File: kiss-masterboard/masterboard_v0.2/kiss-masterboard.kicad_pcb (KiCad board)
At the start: 2 copper layers, 187 x 152 mm, 185 parts, among them J1 Cubebatt_host, J10 CRESET, J11 Jumper, J12 Jumper, J13 Conn_02x08_Odd_Even, J14 Conn_02x08_Odd_Even, J15 jmp, J16 jmp, J17 gain_jumper, J18 Speaker, J2 Conn_01x02, J3 Conn_01x02, J4 Conn_01x02, J5 Conn_01x02, J6 Conn_01x02, J7 Conn_01x02, J8 Jumper, J9 jmp, P2 CONN_02X20, U1 TPS54327, U10 CSD86360Q5D, U12 1V2, U13 SN74LVC8T245, U14 W25Q, U15 MPU-9250, U16 ADS1000, U17 12MHz, U2 SN74LVC8T245, U3 3.3V, U4 ICE40UP5k-SG48, U5 SN74LVC8T245, U6 MAX98357, U7 SPH0645LM4H, U9 TPS53819A

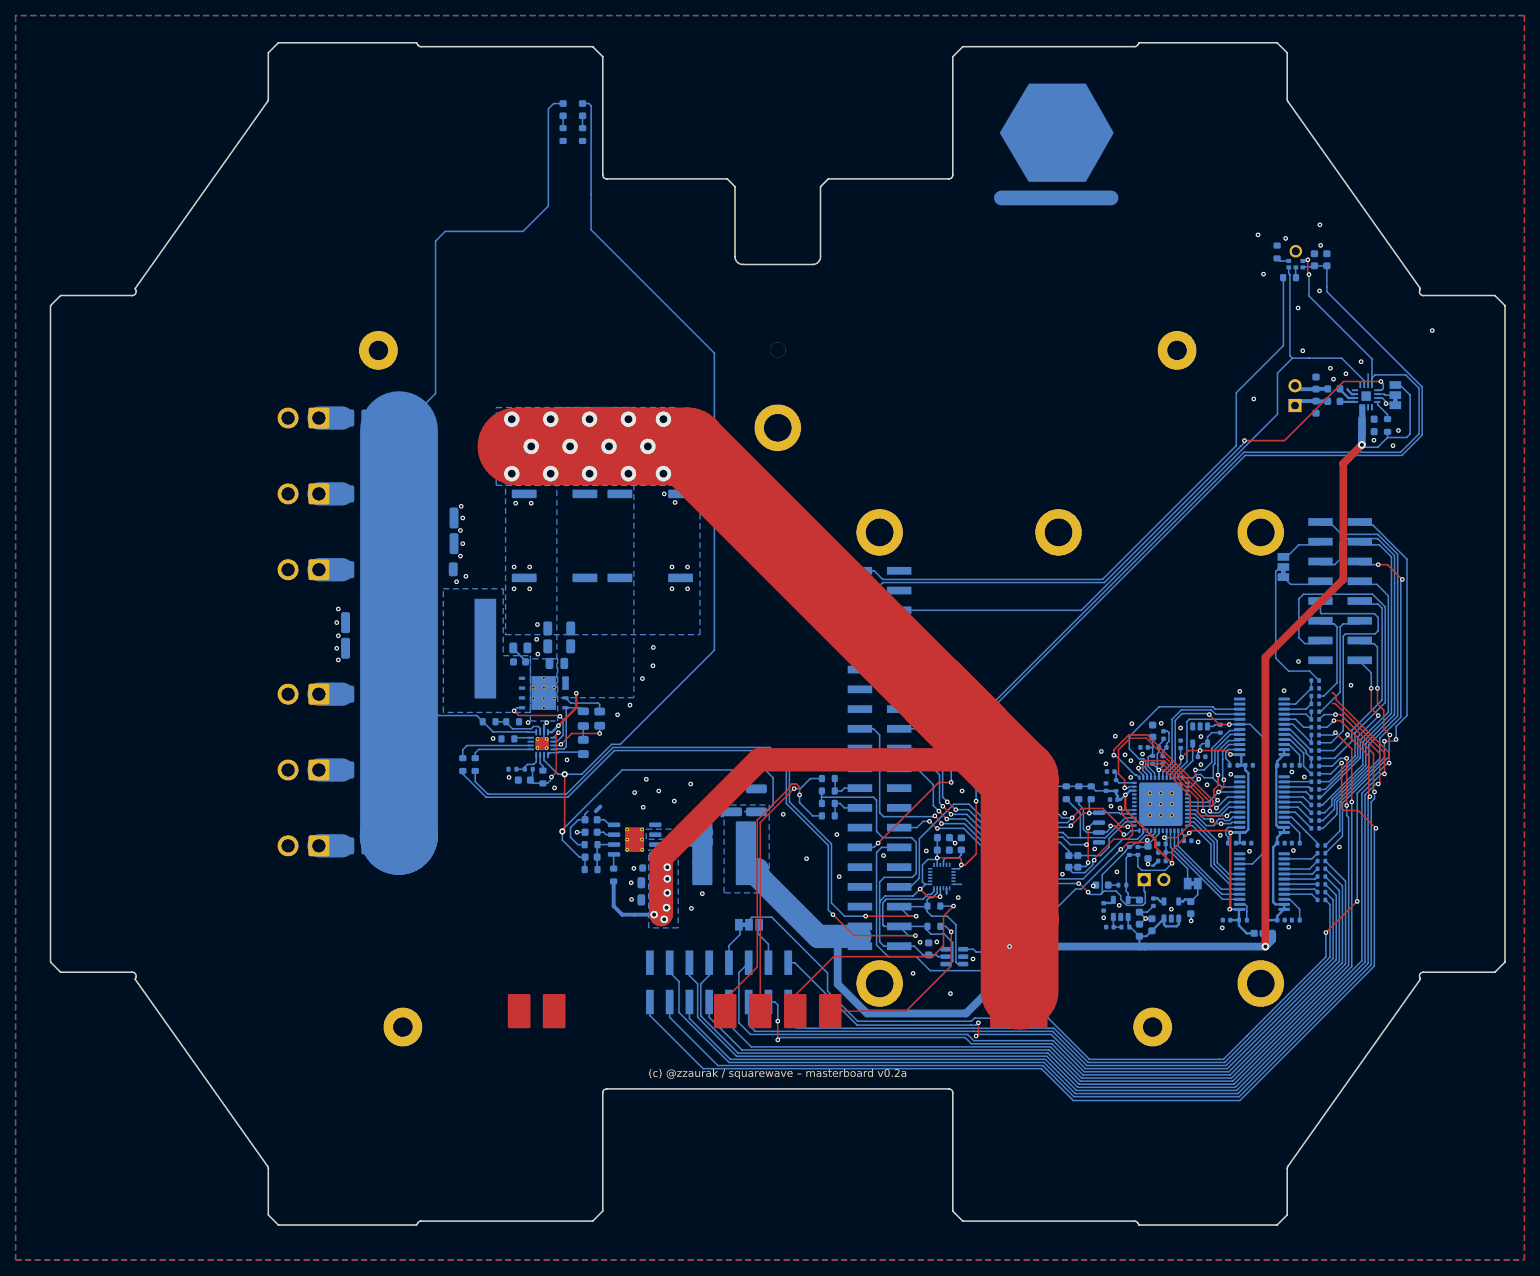
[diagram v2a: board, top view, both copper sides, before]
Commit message: replaced symbosl with standart symbols and reduced DRC errorsMAX98357A and TLV75709PDBV symbols
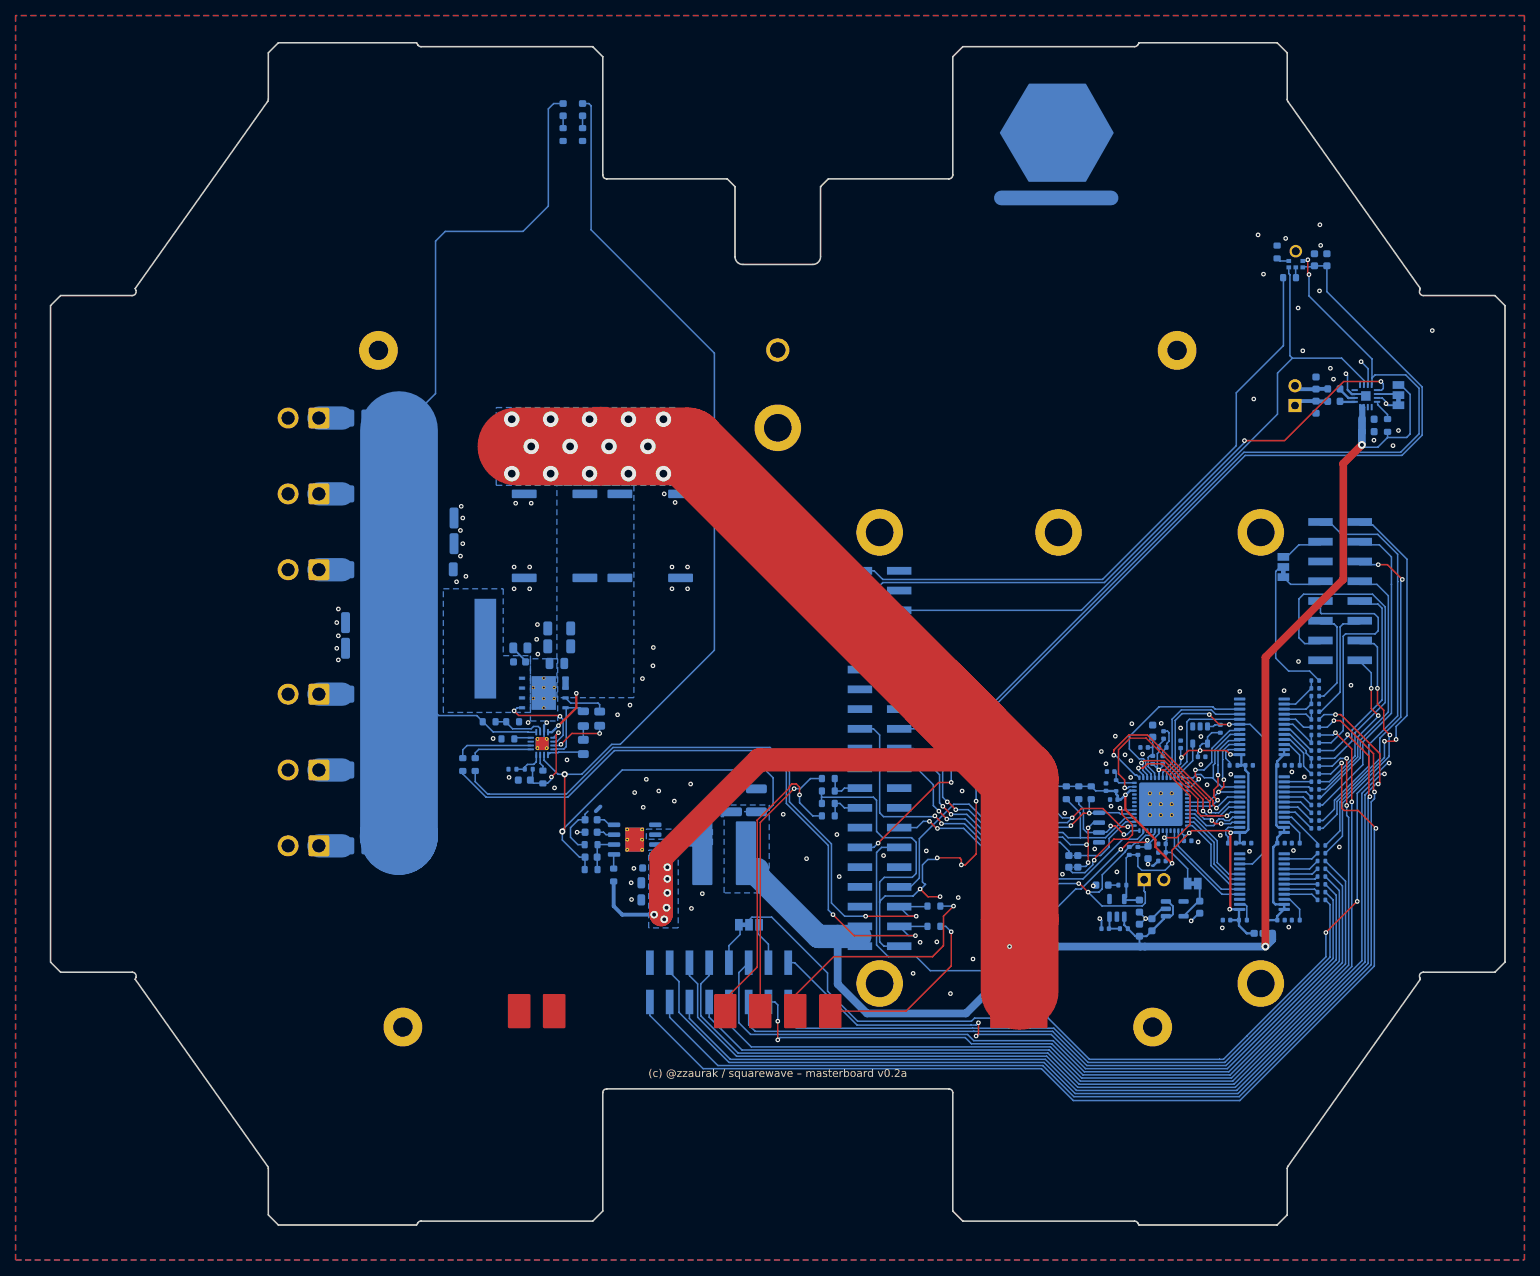
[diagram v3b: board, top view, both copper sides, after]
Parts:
- removed C20, C27: 10n, Capacitor_SMD:C_0402_1005Metric
- removed C66: 10nF, Capacitor_SMD:C_0603_1608Metric
- removed C67, C68, C69: 100nF, Capacitor_SMD:C_0603_1608Metric
- removed J17: gain_jumper, Jumper:SolderJumper-3_P1.3mm_Bridged12_Pad1.0x1.5mm_NumberLabels
- removed R49: 10K 1%, Resistor_SMD:R_0603_1608Metric
- removed R50: 1.78K 1%, Resistor_SMD:R_0603_1608Metric
- removed U12: 1V2, pkl_housings_sot:SOT-23-5
- removed U15: MPU-9250, Sensor_Motion:InvenSense_QFN-24_3x3mm_P0.4mm
- removed U16: ADS1000, Package_TO_SOT_SMD:SOT-23-6
- removed U6: MAX98357, Package_DFN_QFN:TQFN-16-1EP_3x3mm_P0.5mm_EP1.23x1.23mm
- added J19: gain_jumper, Jumper:SolderJumper-3_P1.3mm_Bridged12_Pad1.0x1.5mm_NumberLabels, B.Cu at (187.8, 58.8)
- added U11: TLV75733PDBV, Package_TO_SOT_SMD:SOT-23-5, B.Cu at (151.6, 124.7)
- added U8: TLV75709PDBV, Package_TO_SOT_SMD:SOT-23-5, B.Cu at (159.0, 124.8)
- U3: value 3.3V -> MAX98357A; footprint pkl_housings_sot:SOT-23-5 -> Package_DFN_QFN:TQFN-16-1EP_3x3mm_P0.5mm_EP1.23x1.23mm
- moved U3 73.0 mm to (183.6, 58.9), turned to 180 degrees
- moved C54 1.15 mm to (162.3, 124.6)
- moved C14 0.63 mm to (150.1, 127.4)
- moved R16 0.28 mm to (152.5, 127.4)
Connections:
- C14 pad 1: Net-(U3-EN) -> Net-(U11-EN)
- FB1 pad 2: Net-(U6-OUTP) -> Net-(U3-OUTP)
- FB2 pad 2: Net-(U6-OUTN) -> Net-(U3-OUTN)
- R16 pad 2: Net-(U3-EN) -> Net-(U11-EN)
- R33 pad 1: Net-(U6-~{SD_MODE}) -> Net-(U3-~{SD_MODE})
- U3 pad 1: /5V_switched -> /Digital Audio/DIN
- U3 pad 2: GND -> Net-(J19-C)
- U3 pad 3: Net-(U3-EN) -> GND
- U3 pad 4: Net-(U3-BYP) -> Net-(U3-~{SD_MODE})
- U3 pad 5: +3V3 -> unconnected-(U3-NC-Pad5)
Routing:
- net /FPGA Panel Driver/P2_G1x: track 50.5 -> 0.00 mm
- net /SDA: track 106.8 -> 85.7 mm
- net /SCL: track 97.6 -> 83.6 mm
- net /FPGA Panel Driver/P1_A4x: track 131.4 -> 117.5 mm
- net /FPGA Panel Driver/P1_iR0: track 13.8 -> 0.00 mm
- net /Raspberry Pi/3v3: track 192.3 -> 178.7 mm
- net /FPGA Panel Driver/P1_A3x: track 140.8 -> 128.8 mm
- net Net-(U16-VIN+): track 4.63 -> 0.00 mm
- net /Power_switched: track 197.1 -> 192.9 mm
- net Net-(U15-REGOUT): track 3.80 -> 0.00 mm
- net Net-(U1-SW): track 6.47 -> 2.87 mm
- net GND: track 31.6 -> 34.9 mm, vias 121 -> 118
- net Net-(U11-EN): track 0.00 -> 2.88 mm
- net Net-(U6-~{SD_MODE}): track 2.77 -> 0.00 mm
- net Net-(U3-~{SD_MODE}): track 0.00 -> 2.77 mm
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
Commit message: Fix DRC issues
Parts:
- removed LG1: Logo_DOT1, logos:Logo_Dot_15mm_Text_Mask
- removed LG2: Logo_Squarewave, logos:Logo_Squarewave_Text_15mm_Silks
- J11, J12: footprint pkl_jumpers:J_NC_0603_15 -> Jumper:SolderJumper-2_P1.3mm_Bridged2Bar_Pad1.0x1.5mm
- J9: footprint pkl_jumpers:J_NCNO_0903_30 -> Jumper:SolderJumper-3_P1.3mm_Bridged12_Pad1.0x1.5mm
- moved J12 1.50 mm to (146.0, 121.0)
- moved J11 0.40 mm to (146.0, 118.4)
- moved J9 0.20 mm to (170.4, 128.2)
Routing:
- net /FPGA Panel Driver/P2_G1x: track 0.00 -> 44.0 mm, vias 0 -> 2
- net /FPGA Panel Driver/P1_A4x: track 117.5 -> 131.2 mm, vias 3 -> 4
- net /FPGA Panel Driver/P1_iR0: track 0.00 -> 13.7 mm
- net /FPGA Panel Driver/P1_A3x: track 128.8 -> 142.4 mm, vias 1 -> 2
- net /Raspberry Pi/3v3: track 178.7 -> 171.1 mm, vias 5 -> 2
- net GND: track 34.9 -> 38.8 mm, vias 118 -> 117
- net /FPGA Panel Driver/FPGA_SS_PANEL: track 53.2 -> 55.0 mm
- net /FPGA Panel Driver/FLASH_MISO|IO1: track 39.3 -> 40.3 mm
- net /FPGA Panel Driver/P2_B0x: track 40.7 -> 40.0 mm
- net /FPGA Panel Driver/P2_A2x: track 14.8 -> 15.5 mm
- net /Power_switched: track 192.9 -> 192.7 mm, vias 23 -> 22

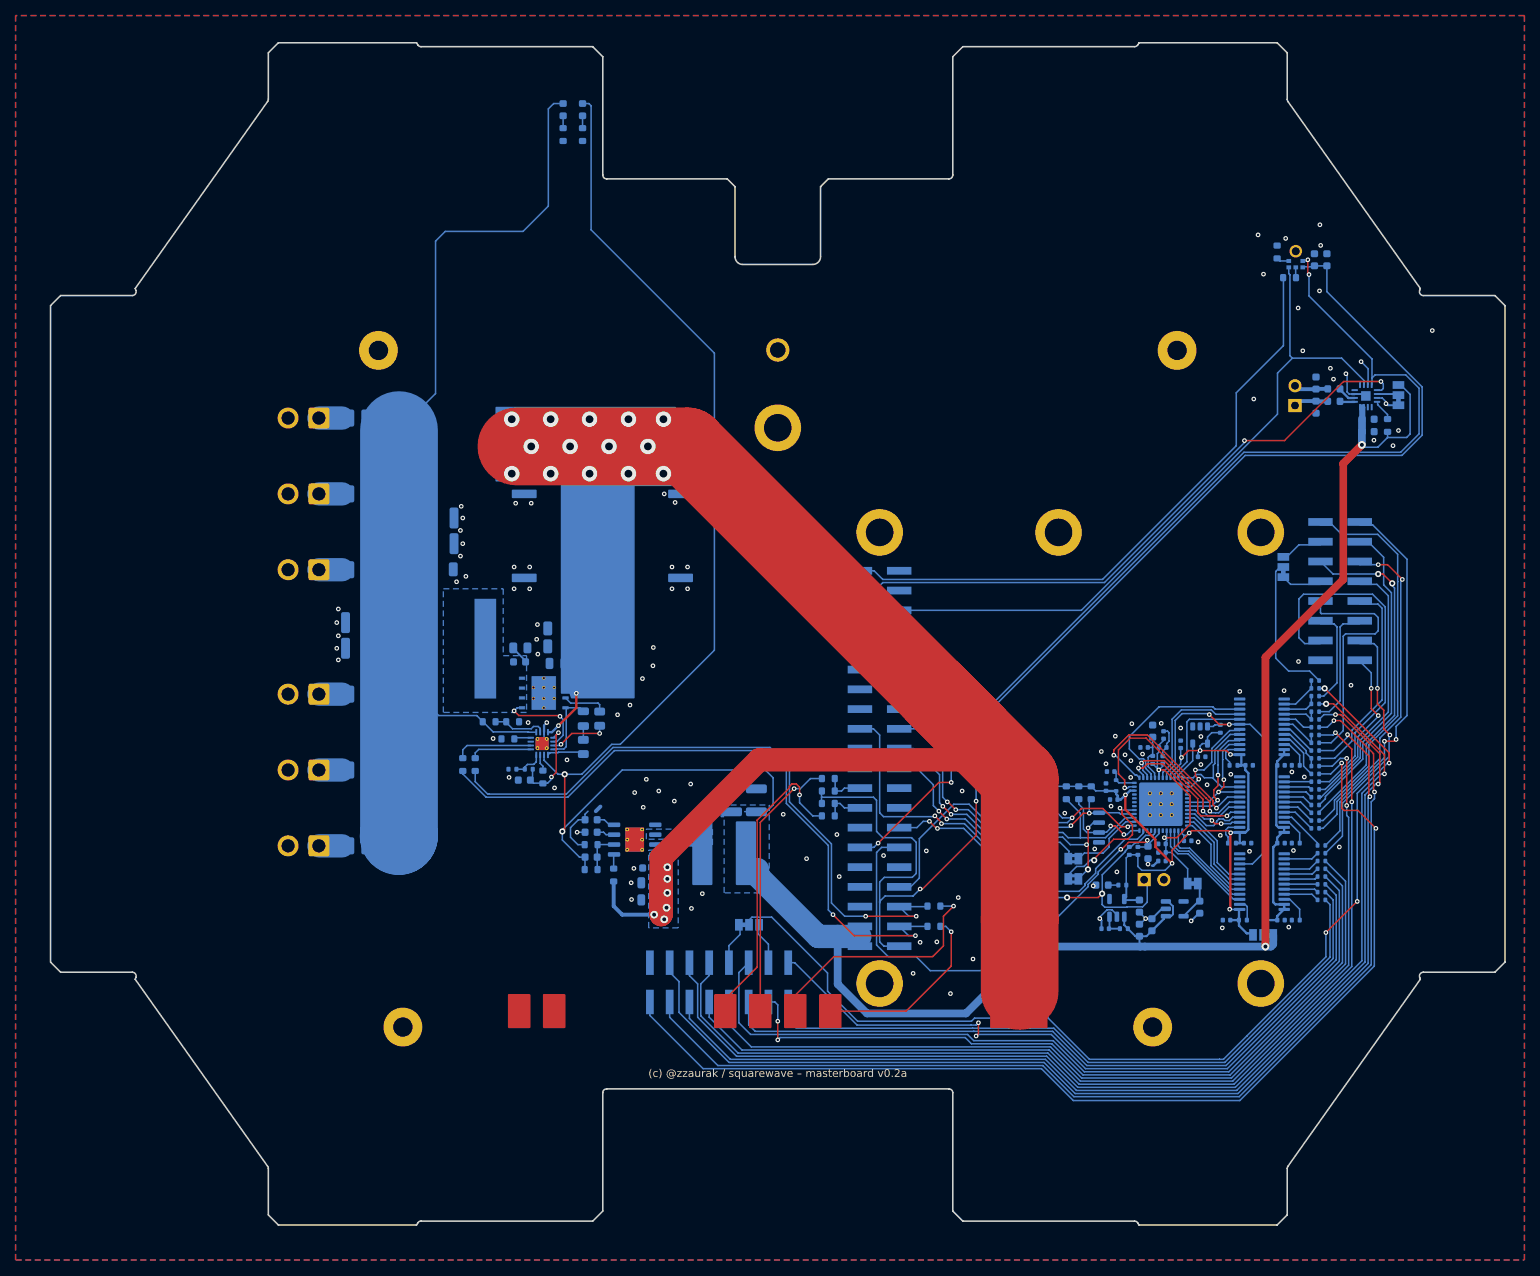
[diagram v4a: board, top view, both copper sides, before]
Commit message: Adjust to new batterypack,
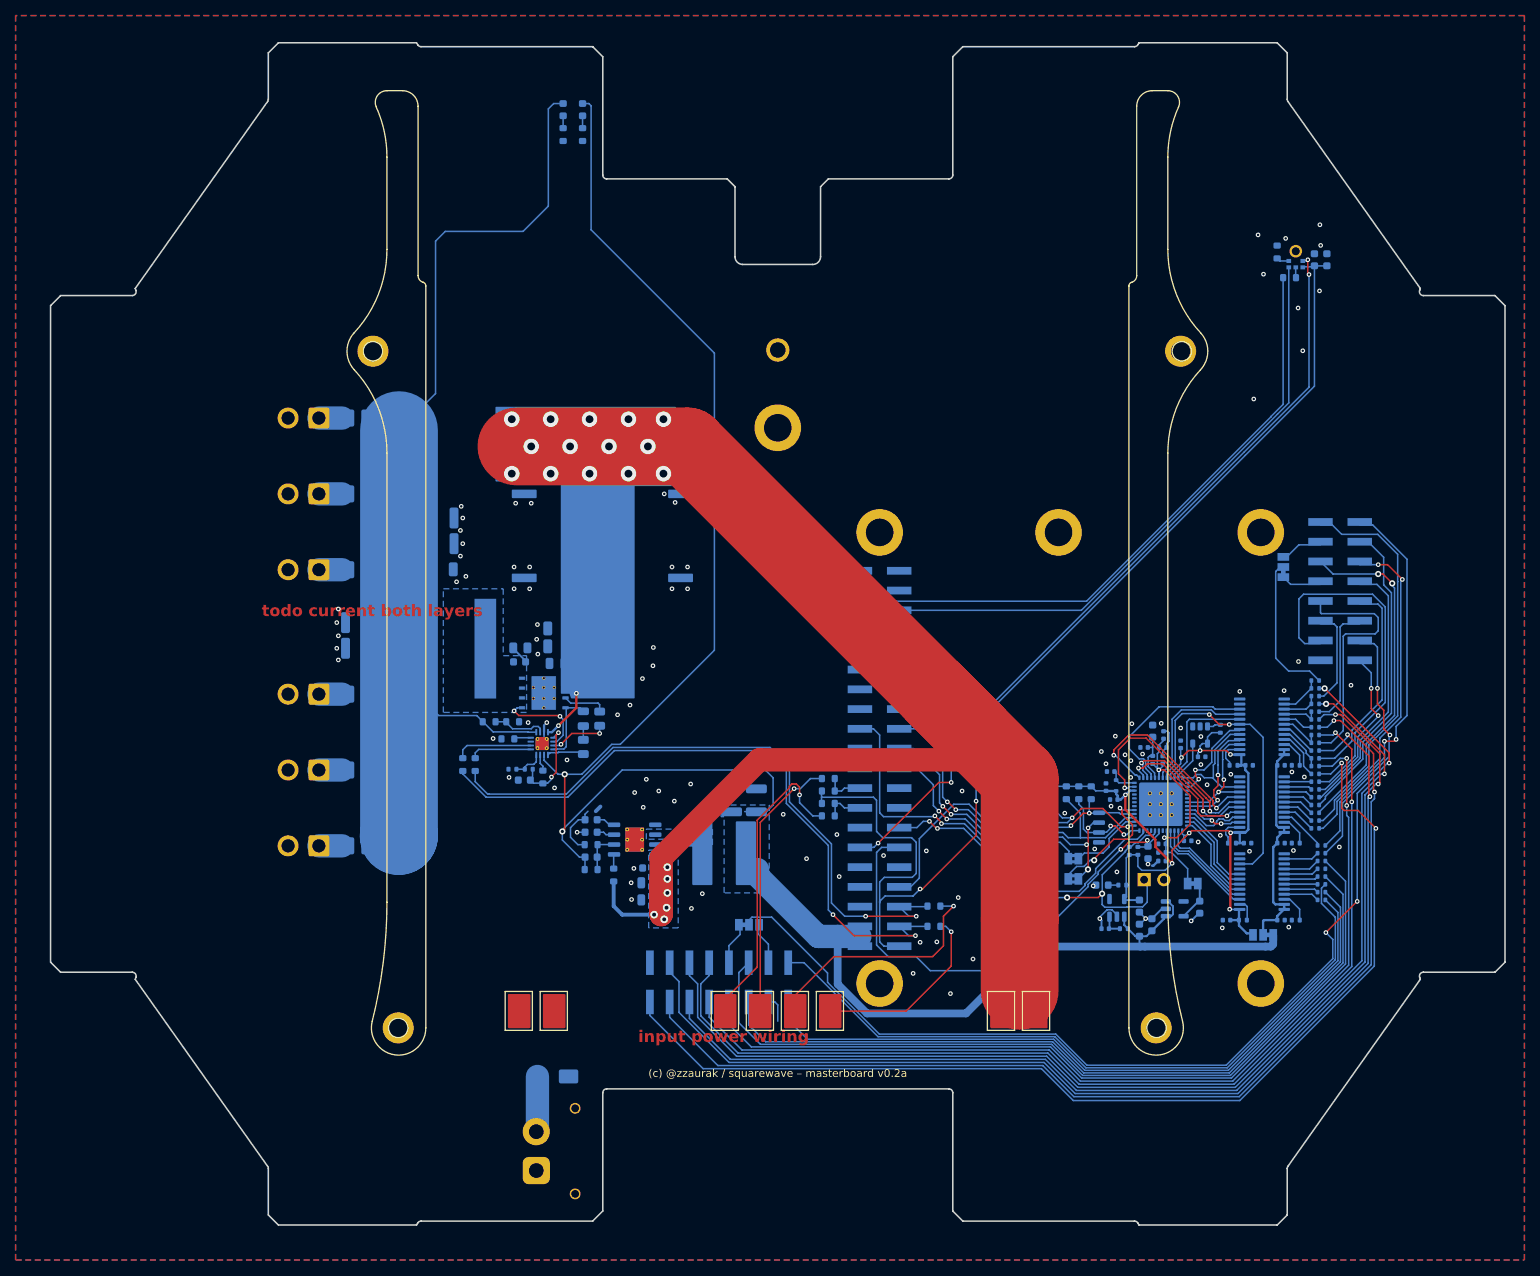
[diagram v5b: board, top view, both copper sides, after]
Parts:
- removed C33: 10uF, Capacitor_SMD:C_0603_1608Metric
- removed C34: 100nF, Capacitor_SMD:C_0603_1608Metric
- removed C37, C38: 220pF, Capacitor_SMD:C_0603_1608Metric
- removed FB1, FB2: Ferrite_Bead_Small, Inductor_SMD:L_0603_1608Metric
- removed J18: Speaker, Connector_PinHeader_2.54mm:PinHeader_1x02_P2.54mm_Vertical
- removed J19: gain_jumper, Jumper:SolderJumper-3_P1.3mm_Bridged12_Pad1.0x1.5mm_NumberLabels
- removed R33: 1M, Resistor_SMD:R_0603_1608Metric
- removed U3: MAX98357A, Package_DFN_QFN:TQFN-16-1EP_3x3mm_P0.5mm_EP1.23x1.23mm
- added D3: 20V 5A, Diode_SMD:D_SMA, B.Cu at (79.1, 146.4)
- added PowerSupply1: Conn_01x02, Connector_AMASS:AMASS_XT30PW-F_1x02_P2.50mm_Horizontal, B.Cu at (77.0, 158.5)
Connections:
- net /Power_switched renamed /Power+
- P2 pad 38: /Digital Audio/DIN -> /Digital Audio/DOUT
- P2 pad 40: /Digital Audio/DOUT -> /Raspberry Pi/PCM_DOUT
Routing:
- net /FPGA Panel Driver/P1_B0x: track 99.5 -> 3.46 mm, vias 2 -> 0
- net /5V_switched: track 350.3 -> 260.5 mm, vias 4 -> 2
- net /Digital Audio/DIN: track 80.1 -> 0.00 mm, vias 2 -> 0
- net /Digital Audio/BCLK: track 129.7 -> 102.2 mm
- net /Raspberry Pi/3v3: track 171.1 -> 148.4 mm
- net GND: track 38.8 -> 27.2 mm, vias 117 -> 108
- net /Digital Audio/LRCLK: track 89.9 -> 78.6 mm
- net Net-(D3-A): track 0.00 -> 7.16 mm
- net Net-(J18-Pin_2): track 4.36 -> 0.00 mm
- net Net-(J18-Pin_1): track 3.60 -> 0.00 mm
- net Net-(U3-~{SD_MODE}): track 2.77 -> 0.00 mm
- net Net-(J19-C): track 2.61 -> 0.00 mm
- net /FPGA Panel Driver/P1_R0x: track 87.5 -> 90.0 mm
- net /FPGA Panel Driver/P1_R1x: track 94.9 -> 97.3 mm
- net Net-(U3-OUTN): track 2.34 -> 0.00 mm
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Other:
- board text added: "input power wiring"
- board text added: "todo current both layers"
